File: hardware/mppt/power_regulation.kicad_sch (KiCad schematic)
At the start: 68 parts, among them IC1501 LMR38010SDDAR, IC1502 TPS2121, J1501 Conn_01x02, U1501 AP63205WU, U1502 TLV75733PDBV

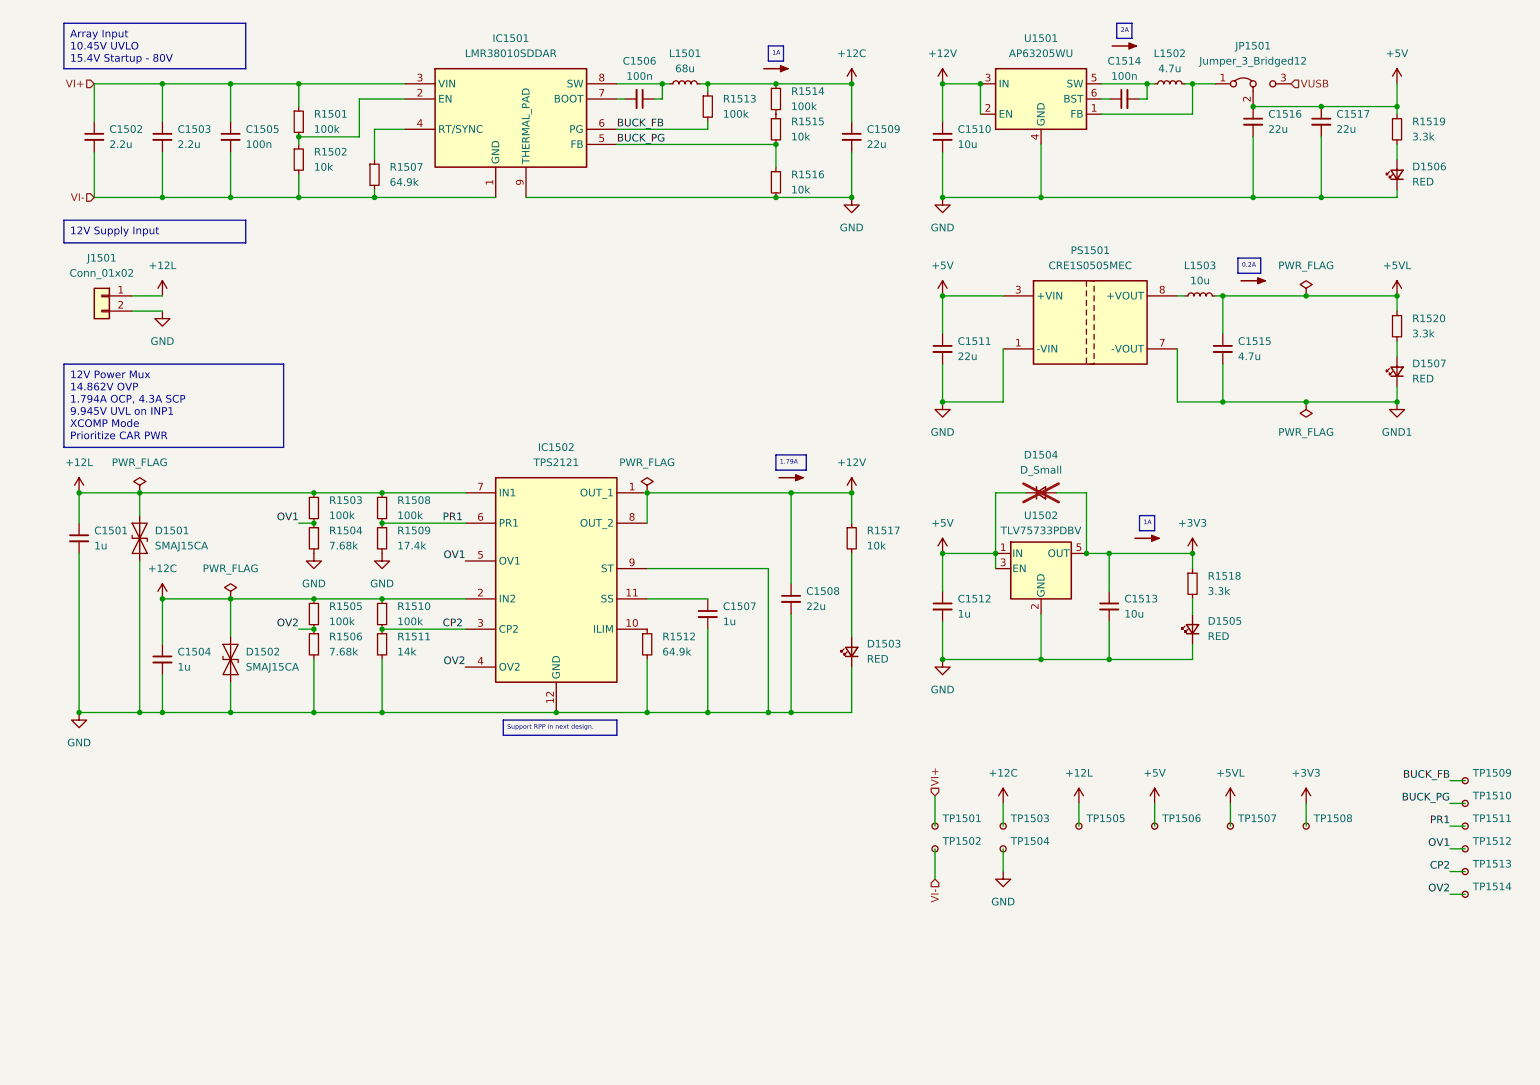
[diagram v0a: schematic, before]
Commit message: update final missing pieces for sch, moving to bom pop
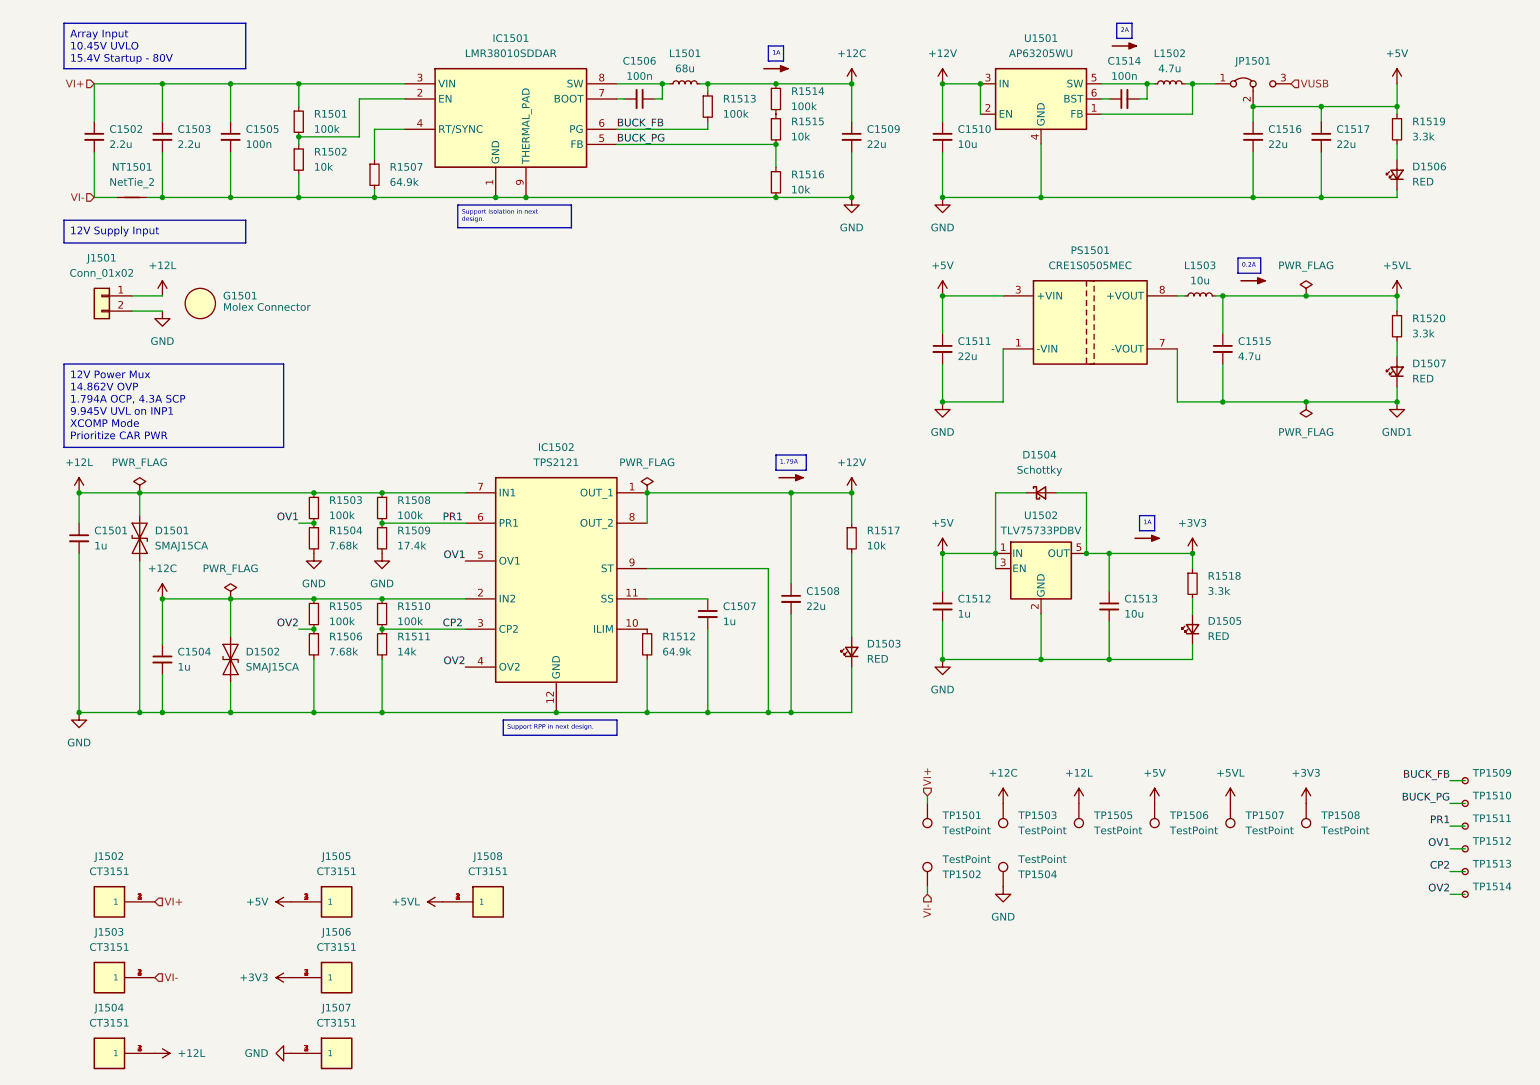
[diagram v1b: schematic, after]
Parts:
- removed TP1501, TP1502, TP1503, TP1504, TP1505, TP1506, TP1507, TP1508: TestPoint_Small, TestPoint:TestPoint_Pad_D1.0mm, symbol Connector:TestPoint_Small
- added G1501: Molex Connector, symbol generic_symbol:Generic_Symbol
- added J1502, J1503, J1504, J1505, J1506, J1507, J1508: CT3151, footprints:caltest_ct3151, symbol caltest_ct3151:CT3151
- added NT1501: NetTie_2, symbol Device:NetTie_2
- added TP1501, TP1502, TP1503, TP1504, TP1505, TP1506, TP1507, TP1508: TestPoint, TestPoint:TestPoint_Keystone_5000-5004_Miniature, symbol Connector:TestPoint
- C1502, C1503: Manufacturer (none) -> TDK; Notes 85V Rating -> 150V Rating
- C1508, C1511, C1516, C1517: Manufacturer (none) -> Samsung Electro-Mechanics
- C1509: Manufacturer (none) -> Samsung Electro-Mechanics; Notes 85V Rating -> 12V Rating
- D1503, D1505, D1506, D1507: footprint (none) -> LED_SMD:LED_0805_2012Metric_Pad1.15x1.40mm_HandSolder
- D1504: value D_Small -> Schottky; symbol Device:D_Small -> Device:D_Schottky_Small; Notes (none) -> 0.55 Forward; now fitted
- J1501: footprint (none) -> Connector_Molex:Molex_Micro-Fit_3.0_43650-0215_1x02_P3.00mm_Vertical; Manufacturer (none) -> Molex; P/N (none) -> 43650-0215
- R1501, R1502, R1503, R1504, R1505, R1506, R1507, R1508, R1509, R1510, R1511, R1512, R1513, R1514, R1515, R1516, R1517, R1518, R1519, R1520: Manufacturer (none) -> Vishay / Dale
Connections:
- net +12C: now also TP1503.1
- net +12L: now also J1504.1, J1504.2 (1), J1504.3 (1), J1504.4 (1), TP1505.1
- net +3V3: now also J1506.1, J1506.2 (1), J1506.3 (1), J1506.4 (1), TP1508.1
- net +5V: now also J1505.1, J1505.2 (1), J1505.3 (1), J1505.4 (1), TP1506.1
- net +5VL: now also J1508.1, J1508.2 (1), J1508.3 (1), J1508.4 (1), TP1507.1
- net GND: now also C1503.2, C1505.2, IC1501.1 (GND), R1502.2, R1507.2, J1507.1, J1507.2 (1), J1507.3 (1), J1507.4 (1), NT1501.1, TP1504.1
- net VI+: now also J1502.1, J1502.2 (1), J1502.3 (1), J1502.4 (1), TP1501.1
- net VI-: now also J1503.1, J1503.2 (1), J1503.3 (1), J1503.4 (1), NT1501.2, TP1502.1; no longer C1503.2, C1505.2, IC1501.1 (GND), R1502.2, R1507.2
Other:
- moved on the sheet: C1516, C1517

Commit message: bom consolidated, starting layout
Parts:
- removed J1505, J1506, J1507, J1508: CT3151, footprints:caltest_ct3151, symbol caltest_ct3151:CT3151
- added G1502: Jumper, symbol generic_symbol:Generic_Symbol
- C1501, C1504, C1507, C1512: footprint (none) -> Capacitor_SMD:C_0603_1608Metric_Pad1.08x0.95mm_HandSolder; Manufacturer Samsung Electro-Mechanics -> TDK; P/N (none) -> CGA3E1X7R1V105K080AC
- C1502, C1503: footprint (none) -> Capacitor_SMD:C_2220_5750Metric_Pad1.97x5.40mm_HandSolder; P/N (none) -> CGA9P3X7T2E225K250KA
- C1505: footprint (none) -> Capacitor_SMD:C_1206_3216Metric_Pad1.33x1.80mm_HandSolder; Manufacturer Samsung Electro-Mechanics -> TDK; P/N (none) -> CGA5L3X7R2E104K160AA
- C1506, C1514: footprint (none) -> Capacitor_SMD:C_0402_1005Metric_Pad0.74x0.62mm_HandSolder; Manufacturer Samsung Electro-Mechanics -> TDK; P/N (none) -> CGA2B3X7R1H104K050BB
- C1508, C1509, C1511, C1516, C1517: footprint (none) -> Capacitor_SMD:C_1210_3225Metric_Pad1.33x2.70mm_HandSolder; Manufacturer Samsung Electro-Mechanics -> TDK; P/N (none) -> CGA6P3X7R1E226M250AB
- C1510, C1513: footprint (none) -> Capacitor_SMD:C_1206_3216Metric_Pad1.33x1.80mm_HandSolder; Manufacturer Samsung Electro-Mechanics -> TDK; P/N (none) -> CGA5L1X7R1E106K160AC
- C1515: footprint (none) -> Capacitor_SMD:C_0805_2012Metric_Pad1.18x1.45mm_HandSolder; Manufacturer Samsung Electro-Mechanics -> TDK; P/N (none) -> CGA4J1X7R1E475K125AC
- D1501, D1502: footprint (none) -> Diode_SMD:D_SMA_Handsoldering; Manufacturer (none) -> Diodes Incorporated; P/N (none) -> SMAJ15CAQ-13-F
- D1503, D1505, D1506, D1507: Manufacturer (none) -> Kingbright; P/N (none) -> APT2012SURCK
- D1504: footprint (none) -> Diode_SMD:D_SOD-123F; Manufacturer (none) -> Diodes Incorporated; Notes 0.55 Forward -> (none); P/N (none) -> SBR3U40S1F-7
- L1501: footprint (none) -> Inductor_SMD:L_Bourns_SRN6045TA; Manufacturer (none) -> Bourns; P/N (none) -> SRN6045TA-680M
- L1502: footprint (none) -> Inductor_SMD:L_Bourns_SRN6045TA; Manufacturer (none) -> Bourns; P/N (none) -> SRN6045TA-4R7M
- L1503: footprint (none) -> Inductor_SMD:L_Bourns_SRN6045TA; Manufacturer Samsung Electro-Mechanics -> Bourns; P/N (none) -> SRN6045TA-100M
- NT1501: footprint (none) -> NetTie:NetTie-2_SMD_Pad2.0mm
- R1501, R1503, R1505, R1508, R1510, R1513, R1514: footprint (none) -> Resistor_SMD:R_0603_1608Metric_Pad0.98x0.95mm_HandSolder; P/N (none) -> CRCW0603100KFKEA
- R1502, R1515, R1516, R1517: footprint (none) -> Resistor_SMD:R_0603_1608Metric_Pad0.98x0.95mm_HandSolder; P/N (none) -> CRCW060310K0FKEA
- R1504, R1506: footprint (none) -> Resistor_SMD:R_0603_1608Metric_Pad0.98x0.95mm_HandSolder; P/N (none) -> CRCW06037K68FKEA
- R1507, R1512: footprint (none) -> Resistor_SMD:R_0603_1608Metric_Pad0.98x0.95mm_HandSolder; P/N (none) -> CRCW060364K9FKEA
- R1509: footprint (none) -> Resistor_SMD:R_0603_1608Metric_Pad0.98x0.95mm_HandSolder; P/N (none) -> CRCW060317K4FKEA
- R1511: footprint (none) -> Resistor_SMD:R_0603_1608Metric_Pad0.98x0.95mm_HandSolder; P/N (none) -> CRCW060314K0FKEA
- R1518, R1519, R1520: footprint (none) -> Resistor_SMD:R_0603_1608Metric_Pad0.98x0.95mm_HandSolder; P/N (none) -> CRCW06033K30FKEA
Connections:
- net GND: no longer C1503.2, C1505.2
- net VI-: now also C1503.2, C1505.2

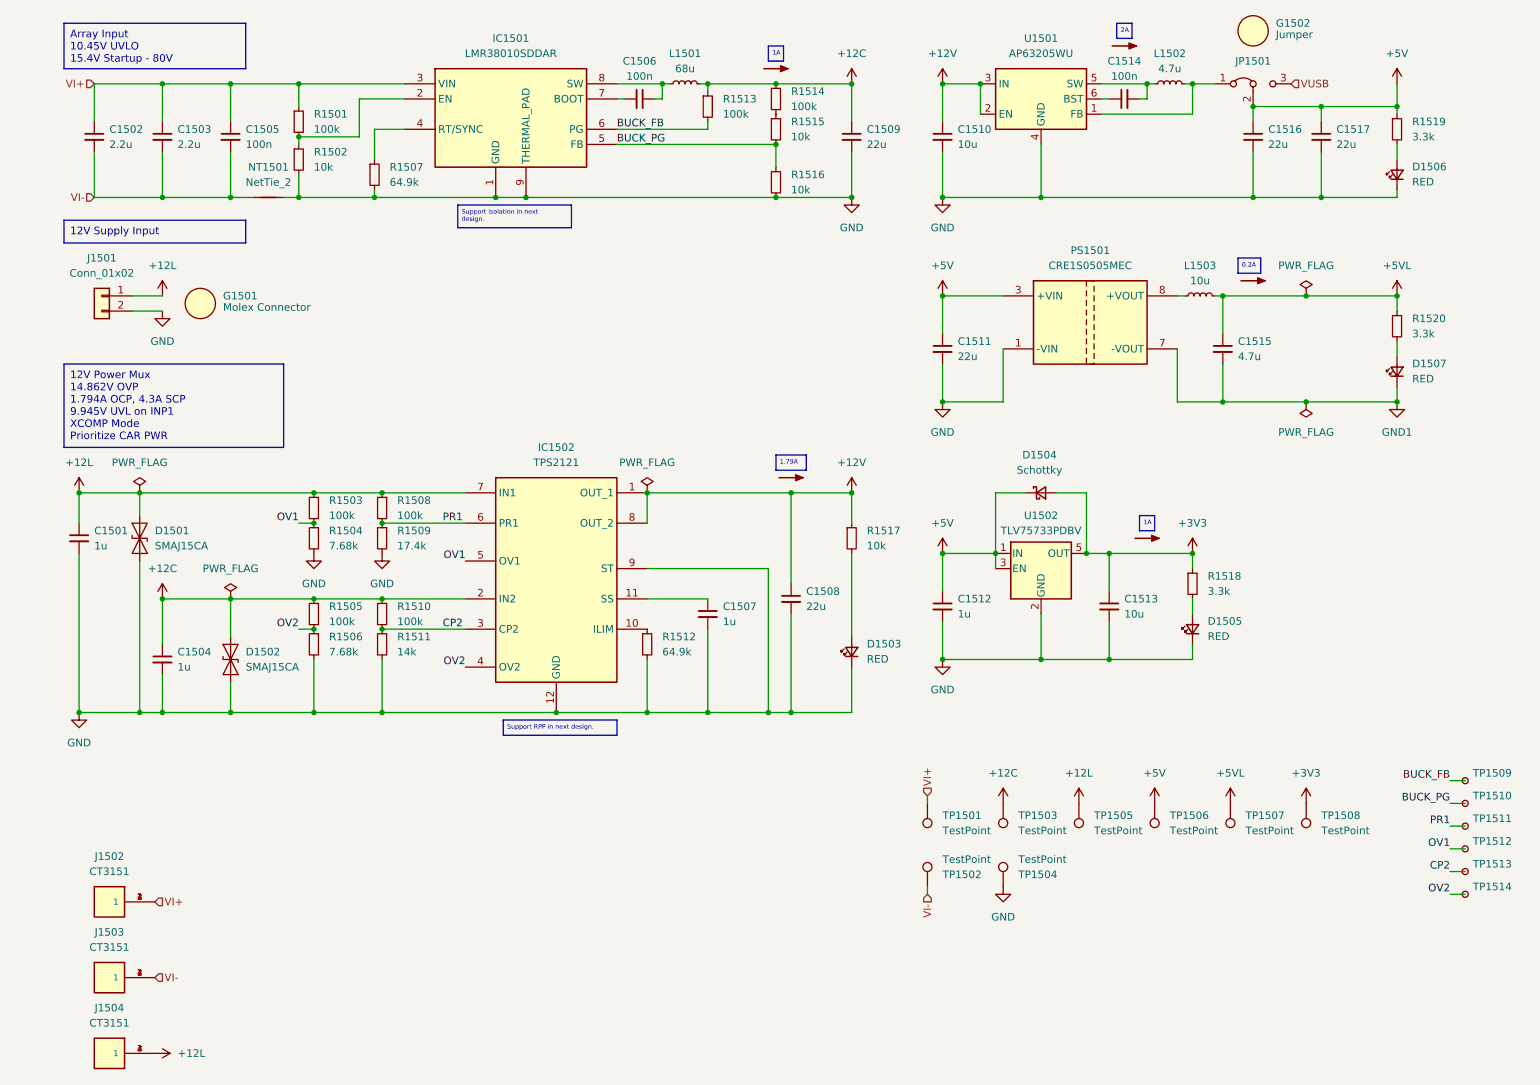
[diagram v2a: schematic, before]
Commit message: PCB variant for power regulation breakout.
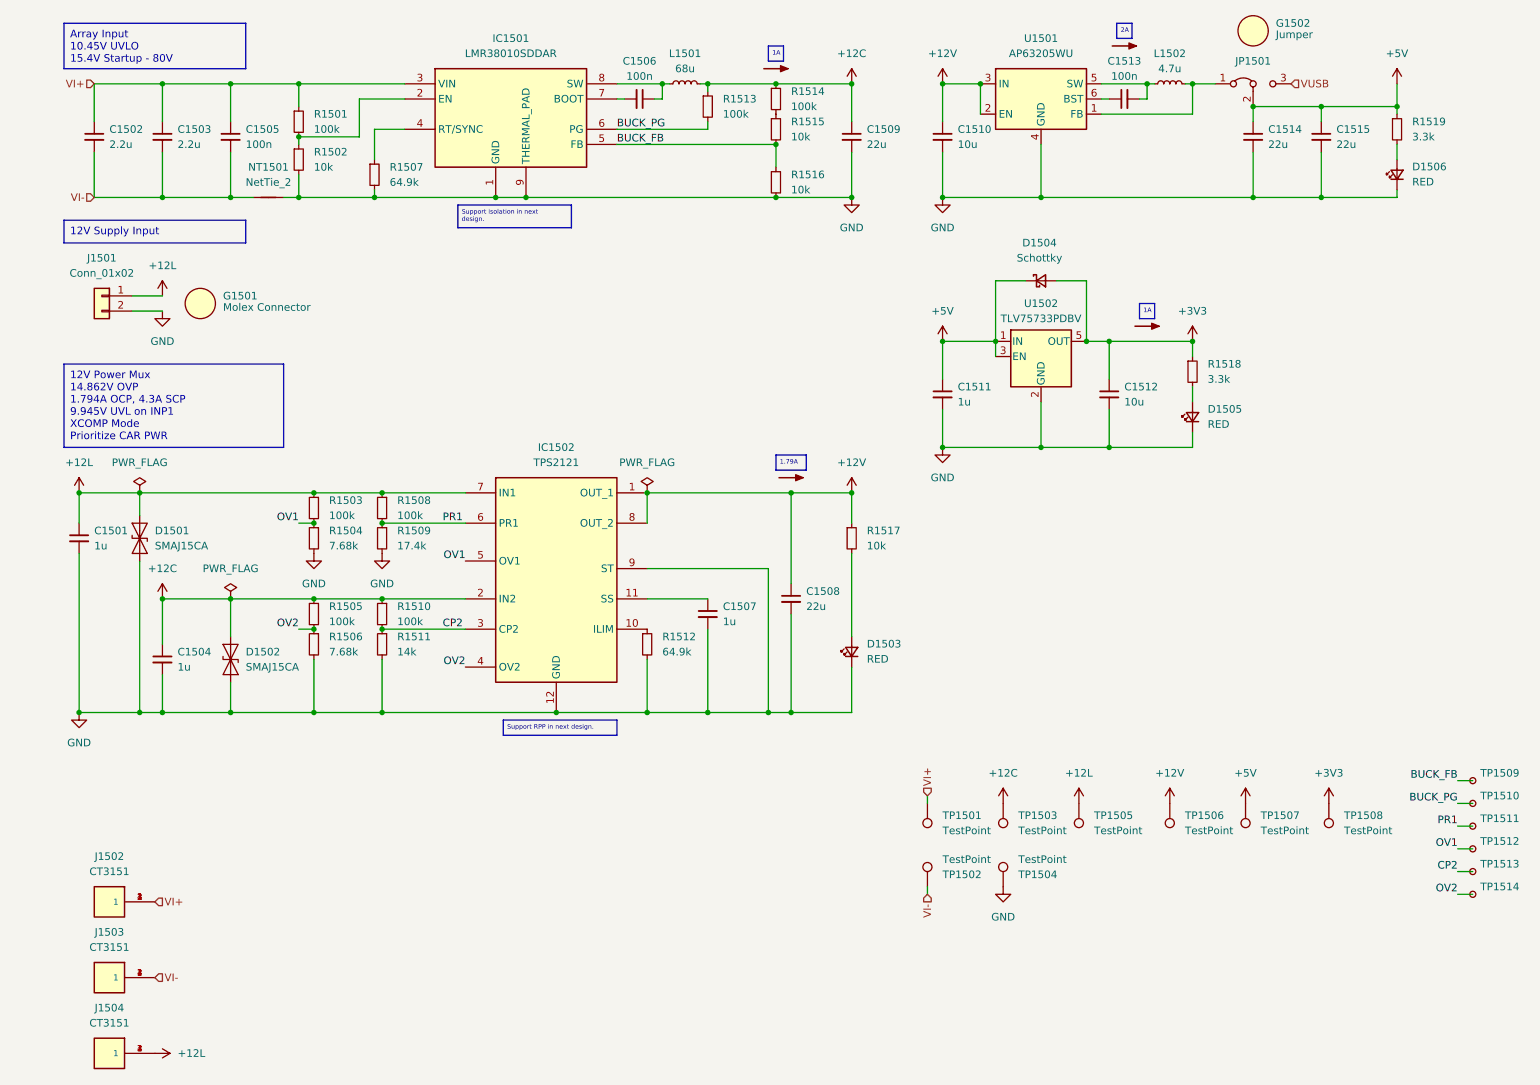
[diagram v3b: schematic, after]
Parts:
- removed C1511: 22u, Capacitor_SMD:C_1210_3225Metric_Pad1.33x2.70mm_HandSolder, symbol Device:C_Small
- removed C1515: 4.7u, Capacitor_SMD:C_0805_2012Metric_Pad1.18x1.45mm_HandSolder, symbol Device:C_Small
- removed D1507: RED, LED_SMD:LED_0805_2012Metric_Pad1.15x1.40mm_HandSolder, symbol Device:LED_Small
- removed L1503: 10u, Inductor_SMD:L_Bourns_SRN6045TA, symbol Device:L_Small
- removed PS1501: CRE1S0505MEC, footprints:murata_CRE1_S0505MEC, symbol murata_CRE1_S0505MEC:CRE1S0505MEC
- removed R1520: 3.3k, Resistor_SMD:R_0603_1608Metric_Pad0.98x0.95mm_HandSolder, symbol Device:R_Small
- removed TP1507: TestPoint, TestPoint:TestPoint_Keystone_5000-5004_Miniature, symbol Connector:TestPoint
- added TP1506: TestPoint, TestPoint:TestPoint_Keystone_5000-5004_Miniature, symbol Connector:TestPoint
- D1501, D1502: footprint Diode_SMD:D_SMA_Handsoldering -> Diode_SMD:D_SMA
- renumbered C1512 to C1511, C1513 to C1512, C1514 to C1513, C1516 to C1514, C1517 to C1515, TP1506 to TP1507
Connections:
- net +12V: now also TP1506.1
- net BUCK_FB: now also IC1501.5 (FB), R1515.2, R1516.1; no longer IC1501.6 (PG), R1513.2
- net BUCK_PG: now also IC1501.6 (PG), R1513.2; no longer IC1501.5 (FB), R1515.2, R1516.1
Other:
- moved on the sheet: C1511, C1512, D1504, D1505, R1518, TP1507, TP1508, TP1509, TP1510, TP1511, TP1512, TP1513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
